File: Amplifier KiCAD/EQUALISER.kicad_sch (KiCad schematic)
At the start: 43 parts, among them U1 TL081, U2 TL081, U3 TL081, U4 TL081, U5 TL081, U6 TL081

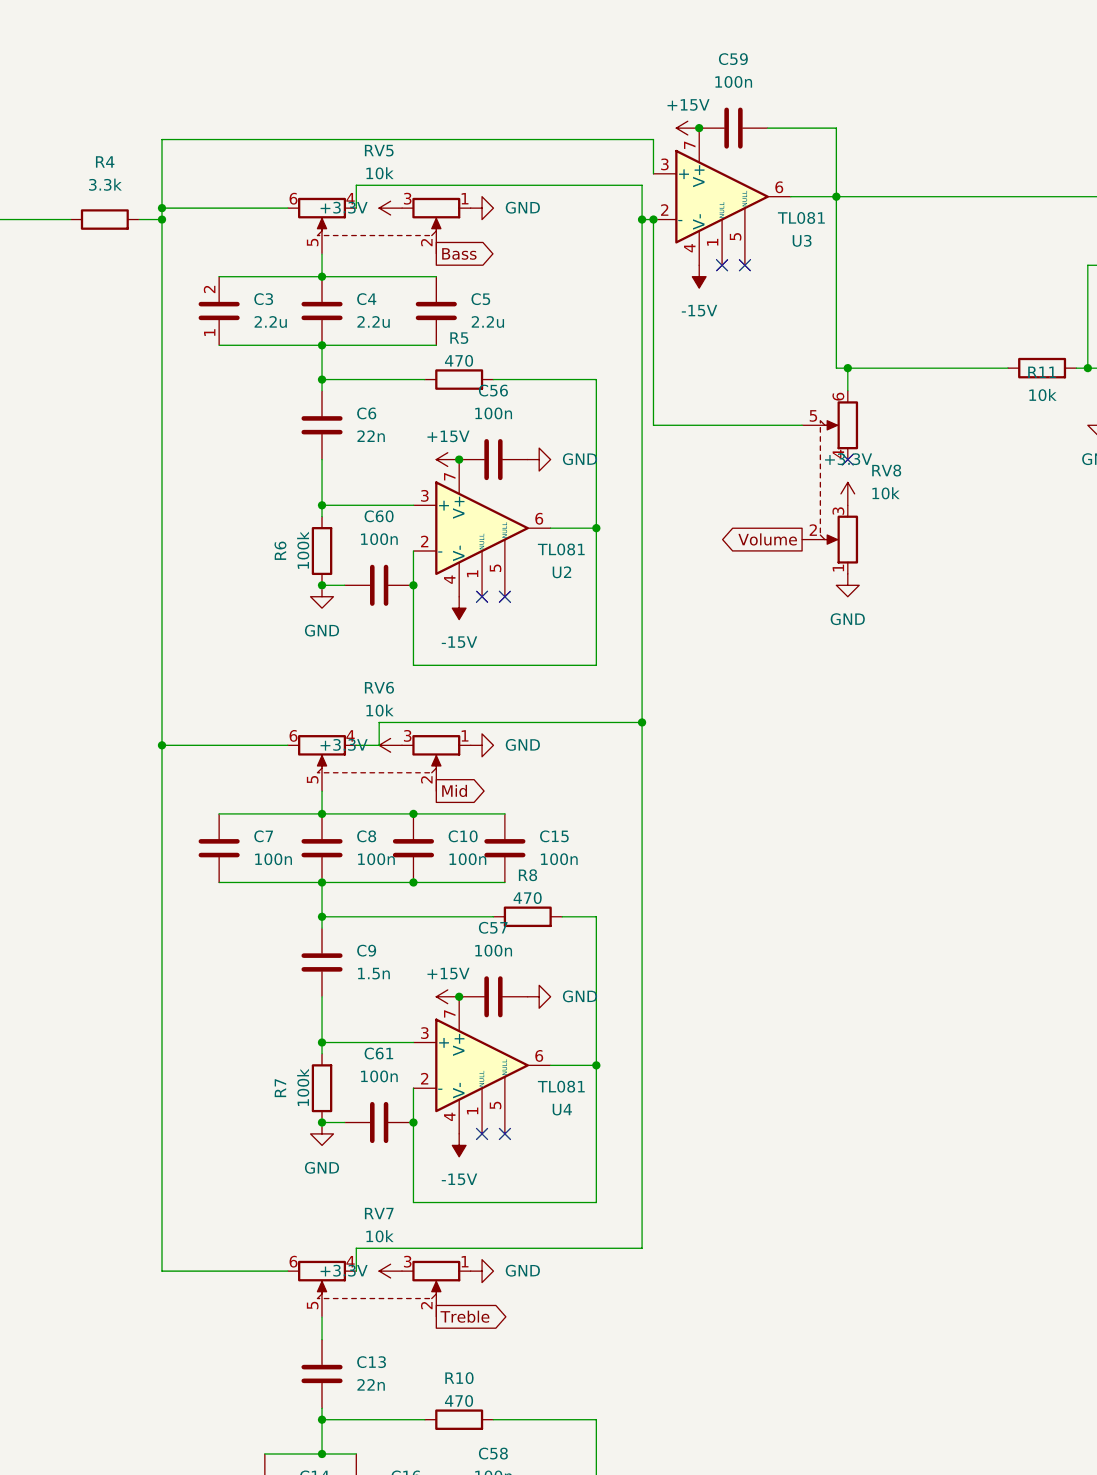
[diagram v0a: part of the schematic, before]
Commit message: Completed placement of equaliser; Tidied up soldermask; Started STM32 placement
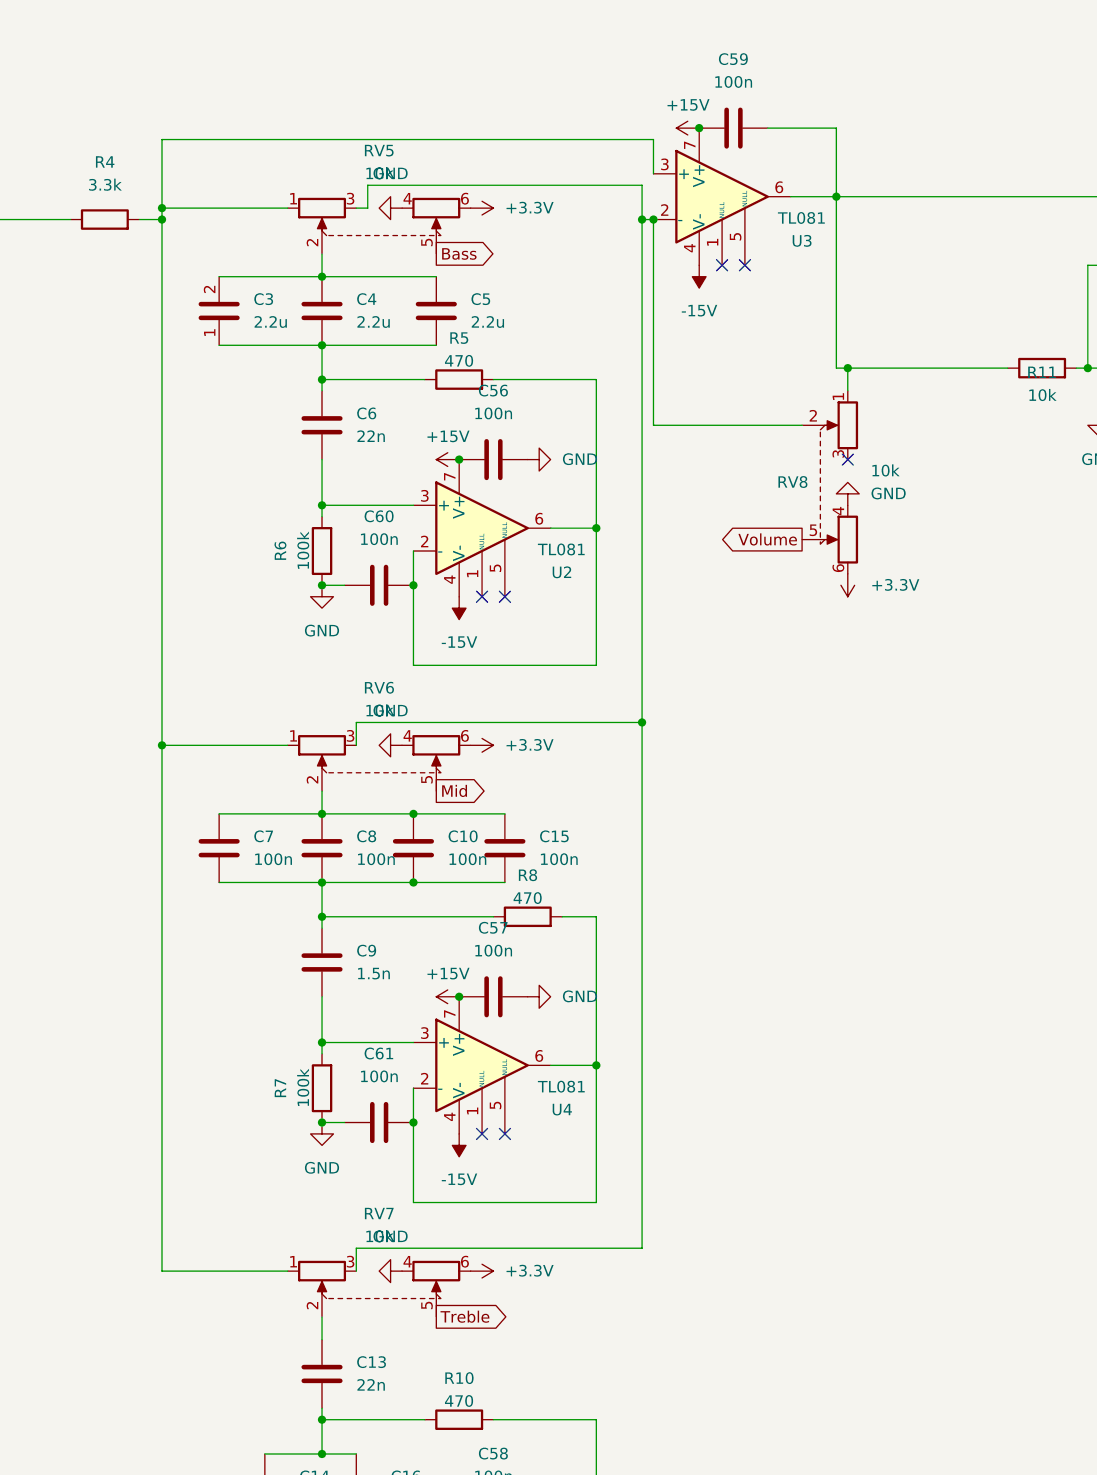
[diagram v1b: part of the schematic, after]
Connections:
- net +3.3V: now also RV5.6, RV6.6, RV7.6, RV8.6; no longer RV5.3, RV6.3, RV7.3, RV8.3
- net Bass: now also RV5.5; no longer RV5.2
- net GND: now also RV5.4, RV6.4, RV7.4, RV8.4; no longer RV5.1, RV6.1, RV7.1, RV8.1
- net In+: now also RV8.1; no longer RV8.6
- net Mid: now also RV6.5; no longer RV6.2
- net Treble: now also RV7.5; no longer RV7.2
- net Volume: now also RV8.5; no longer RV8.2
- net at C10.1, C15.1, C7.1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: now also RV6.2; no longer RV6.5
- net at C3.2, C4.2, C5.2: now also RV5.2; no longer RV5.5
- net at C13.1: now also RV7.2; no longer RV7.5
- new net: R4.2, RV5.1, RV6.1, RV7.1, U3.3 (+)
- new net: RV5.3, RV6.3, RV7.3, RV8.2, U3.2 (-)
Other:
- moved on the sheet: RV5, RV6, RV7
